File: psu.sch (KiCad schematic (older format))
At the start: 8 parts

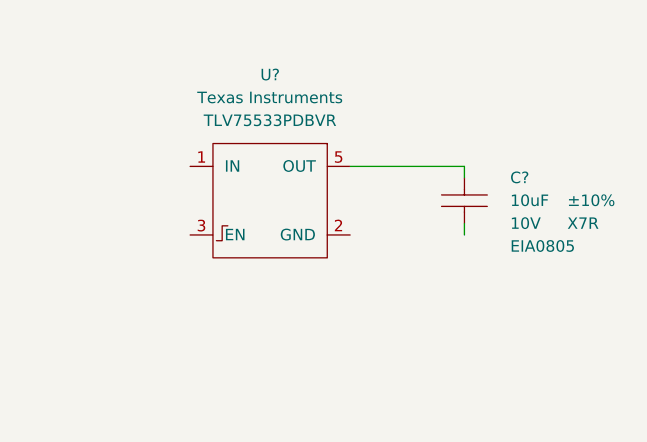
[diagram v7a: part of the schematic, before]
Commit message: Add PSU to GND jumper.
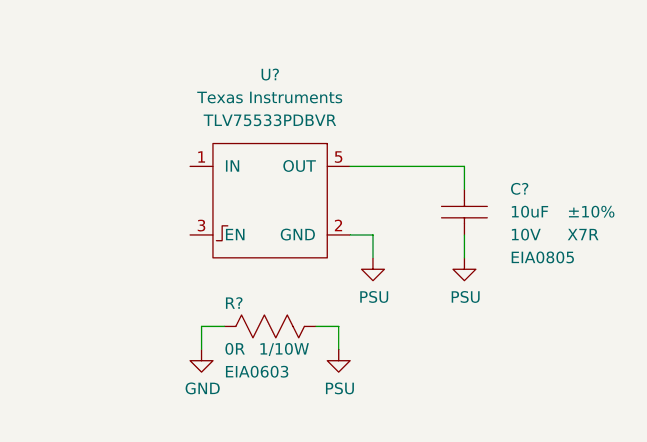
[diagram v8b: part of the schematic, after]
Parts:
- added R?: RES-EIA0603, footprints_generic:RESC160X85X55L30N, symbol gz_Chip-Resistors-Surface-Mount:RES-EIA0603
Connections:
- net labels added: PSU
- wire segments 19 -> 25
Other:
- moved on the sheet: C?
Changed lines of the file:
@@
 L gz_Ceramic-Capacitors:CAP-EIA0805 C?
 U 1 1 6046210B
-P 9250 1850
-F 0 "C?" V 9150 2050 50  0000 L CNN
-F 1 "CAP-EIA0805" H 9650 2950 50  0001 L CNN
-F 2 "footprints_generic:CAPC200X125X110L50N" H 5950 6200 50  0001 L CNN
-F 3 "https://www.kemet.com/specsheet/C0805C106K8RACTU" H 5950 6300 50  0001 L CNN
-F 4 "399-7411-1-ND" H 9650 2850 50  0001 L CNN "Digi-Key_PN"
-F 5 "KEMET" H 9650 2750 50  0001 L CNN "Manufacturer"
-F 6 "C0805C106K8RACTU" H 9650 2650 50  0001 L CNN "MPN"
-F 7 "Capacitors" H 5950 6600 50  0001 L CNN "Category"
-F 8 "Ceramic Capacitors" H 5950 6700 50  0001 L CNN "Family"
-F 9 "10uF" V 9250 2050 50  0000 L CNN "Capacitance"
-F 10 "±10%" V 9250 2300 50  0000 L CNN "Tolerance"
-F 11 "10V" V 9350 2050 50  0000 L CNN "Voltage"
-F 12 "X7R" V 9350 2300 50  0000 L CNN "Dielectric"
-F 13 "EIA0805" V 9450 2050 50  0000 L CNN "Package"
-	1    9250 1850
+P 9250 1900
+F 0 "C?" V 9150 2100 50  0000 L CNN
+F 1 "CAP-EIA0805" H 9650 3000 50  0001 L CNN
+F 2 "footprints_generic:CAPC200X125X110L50N" H 5950 6250 50  0001 L CNN
+F 3 "https://www.kemet.com/specsheet/C0805C106K8RACTU" H 5950 6350 50  0001 L CNN
+F 4 "399-7411-1-ND" H 9650 2900 50  0001 L CNN "Digi-Key_PN"
+F 5 "KEMET" H 9650 2800 50  0001 L CNN "Manufacturer"
+F 6 "C0805C106K8RACTU" H 9650 2700 50  0001 L CNN "MPN"
+F 7 "Capacitors" H 5950 6650 50  0001 L CNN "Category"
+F 8 "Ceramic Capacitors" H 5950 6750 50  0001 L CNN "Family"
+F 9 "10uF" V 9250 2100 50  0000 L CNN "Capacitance"
+F 10 "±10%" V 9250 2350 50  0000 L CNN "Tolerance"
+F 11 "10V" V 9350 2100 50  0000 L CNN "Voltage"
+F 12 "X7R" V 9350 2350 50  0000 L CNN "Dielectric"
+F 13 "EIA0805" V 9450 2100 50  0000 L CNN "Package"
+	1    9250 1900
 	0    1    1    0
 $EndComp
@@
 	8750 1700 9250 1700
 Wire Wire Line
-	9250 1700 9250 1750
+	9250 1700 9250 1800
+$Comp
+L gz_Power-Symbols:PSU #PWR?
+U 1 1 6046924F
+P 9250 2100
+F 0 "#PWR?" H 9250 1850 50  0001 C CNN
+F 1 "PSU" H 9255 1927 50  0000 C CNN
+F 2 "" H 9250 2100 50  0001 C CNN
+F 3 "" H 9250 2100 50  0001 C CNN
+	1    9250 2100
+	1    0    0    -1
+$EndComp
+$Comp
+L gz_Power-Symbols:PSU #PWR?
+U 1 1 6046A224
+P 8700 2500
+F 0 "#PWR?" H 8700 2250 50  0001 C CNN
+F 1 "PSU" H 8705 2327 50  0000 C CNN
+F 2 "" H 8700 2500 50  0001 C CNN
+F 3 "" H 8700 2500 50  0001 C CNN
+	1    8700 2500
+	1    0    0    -1
+$EndComp
+$Comp
+L gz_Power-Symbols:GND #PWR?
+U 1 1 6046B337
+P 8100 2500
+F 0 "#PWR?" H 8100 2250 50  0001 C CNN
+F 1 "GND" H 8105 2327 50  0000 C CNN
+F 2 "" H 8100 2500 50  0001 C CNN
+F 3 "" H 8100 2500 50  0001 C CNN
+	1    8100 2500
+	1    0    0    -1
+$EndComp
+$Comp
+L gz_Chip-Resistors-Surface-Mount:RES-EIA0603 R?
+U 1 1 6046C6CC
+P 8400 2400
+F 0 "R?" H 8200 2500 50  0000 L CNN
+F 1 "RES-EIA0603" H 9200 3300 50  0001 L CNN
+F 2 "footprints_generic:RESC160X85X55L30N" H 5100 6750 50  0001 L CNN
+F 3 "http://industrial.panasonic.com/www-cgi/jvcr13pz.cgi?E+PZ+3+AOA0001+ERJ3GEY0R00V+7+WW" H 5100 6850 50  0001 L CNN
+F 4 "P0.0GCT-ND" H 9200 3200 50  0001 L CNN "Digi-Key_PN"
+F 5 "Panasonic Electronic Components" H 9200 3100 50  0001 L CNN "Manufacturer"
+F 6 "ERJ-3GEY0R00V" H 9200 3000 50  0001 L CNN "MPN"
+F 7 "Resistors" H 5100 7150 50  0001 L CNN "Category"
+F 8 "Chip Resistor - Surface Mount" H 5100 7250 50  0001 L CNN "Family"
+F 9 "0R" H 8200 2300 50  0000 L CNN "Resistance"
+F 10 "N/A" H 8400 2797 50  0001 L CNN "Tolerance"
+F 11 "1/10W" H 8350 2300 50  0000 L CNN "Power"
+F 12 "N/A" H 8400 2615 50  0001 L CNN "Voltage"
+F 13 "EIA0603" H 8200 2200 50  0000 L CNN "Package"
+	1    8400 2400
+	1    0    0    -1
+$EndComp
 Wire Wire Line
-	9250 1950 9250 2000
+	8100 2500 8100 2400
+Wire Wire Line
+	8100 2400 8200 2400
+Wire Wire Line
+	8600 2400 8700 2400
+Wire Wire Line
+	8700 2400 8700 2500
+Wire Wire Line
+	9250 2000 9250 2100
+Wire Wire Line
+	8750 2000 8850 2000
+$Comp
+L gz_Power-Symbols:PSU #PWR?
+U 1 1 60478588
+P 8850 2100
+F 0 "#PWR?" H 8850 1850 50  0001 C CNN
+F 1 "PSU" H 8855 1927 50  0000 C CNN
+F 2 "" H 8850 2100 50  0001 C CNN
+F 3 "" H 8850 2100 50  0001 C CNN
+	1    8850 2100
+	1    0    0    -1
+$EndComp
+Wire Wire Line
+	8850 2000 8850 2100
 $EndSCHEMATC
